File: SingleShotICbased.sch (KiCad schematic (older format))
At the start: 14 parts

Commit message: finished design
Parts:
- added D1, D9: 5.1V, Diode_SMD:D_SOD-123, symbol Device:D_Zener
- added D2, D4, D5, D8: RB751S40T5G, Diode_SMD:D_SOD-523, symbol Device:D_Schottky
- added D3, D6, D7: 2SS100L-W, Diode_SMD:D_SOD-123F, symbol Device:D_Schottky
- added R1: 15K, Resistor_SMD:R_0805_2012Metric_Pad1.15x1.40mm_HandSolder, symbol Device:R
- J1: renamed from J?; value Conn_01x01_Male -> GM_KP_ALIVE; footprint (none) -> Connector_PinHeader_2.54mm:PinHeader_1x01_P2.54mm_Horizontal
- J2: renamed from J?; footprint (none) -> Connector_PinHeader_2.54mm:PinHeader_1x02_P2.54mm_Horizontal
- J3: renamed from J?; value Conn_01x01_Female -> SSR_ANODE; footprint (none) -> Connector_PinHeader_2.54mm:PinHeader_1x01_P2.54mm_Horizontal
- J4: renamed from J?; footprint (none) -> Connector_PinHeader_2.54mm:PinHeader_1x03_P2.54mm_Horizontal
- gave numbers to parts that had none: 10
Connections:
- net Earth: now also C2.2, D1.2 (A), D9.2 (A)
- net LV_BATT+_DIODE: now reaches C1.1, C3.1, U1.1 (IN), U2.1 (IN)
- net LV_BATT+_DIODE: now also D3.1 (K); no longer J2.1 (Pin_1)
- net LIN_TIMER_EN: now reaches U2.2 (EN)
- net LIN_TIMER_EN: now also D6.1 (K), D7.1 (K)
- net LIN_TIMER_VDD: now reaches C4.1, U2.5 (OUT), U2.6 (ADJ/SEN)
- net LIN_TIMER_VDD: now also D5.2 (A); no longer U3.1 (VDD)
- net TIMER_DRVn: now reaches U1.2 (EN), U3.5 (DRVn)
- net LIN_SSR_ANODE: now reaches C2.1, U1.5 (OUT), U1.6 (ADJ/SEN)
- net LIN_SSR_ANODE: now also D4.2 (A)
- net TIMER_DONE: now reaches R4.1, U3.4 (DONE)
- net TIMER_DONE: now also D1.1 (K), R1.1
- net GRND_ESTP: now reaches J4.1 (Pin_1)
- net GRND_ESTP: now also D6.2 (A)
- net PLAT_ESTOP: now reaches J4.2 (Pin_2)
- net PLAT_ESTOP: now also D7.2 (A)
- net TMATICS: now reaches J4.3 (Pin_3)
- net TMATICS: now also D8.2 (A)
- net at J1.1 (Pin_1): now also D2.2 (A), R1.2
- net at J3.1 (Pin_1): now also D2.1 (K), D4.1 (K)
- new net LV_BATT+_RAW: D3.2 (A), J2.1 (Pin_1)
- new net TIMER_VDD: D5.1 (K), D8.1 (K), D9.1 (K), U3.1 (VDD)
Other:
- moved on the sheet: C1, J1, J2, J3, J4, R2, R3, R4, U3

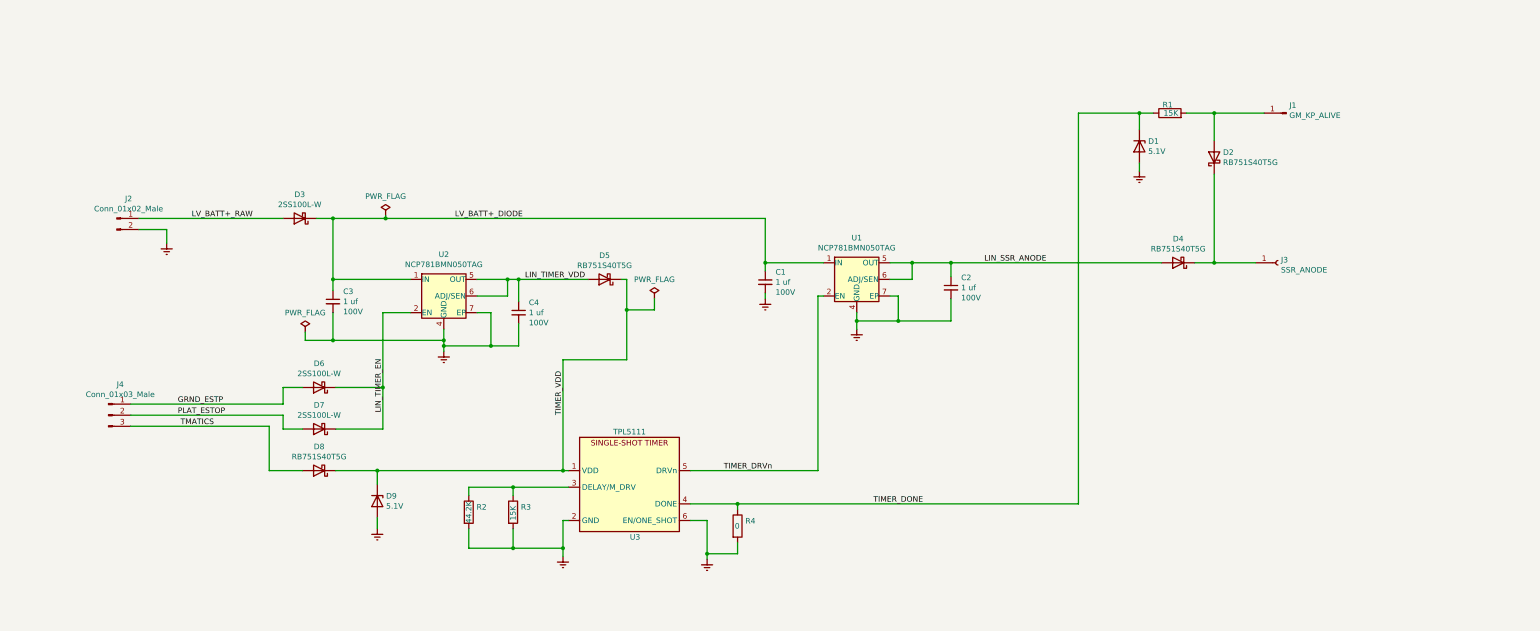
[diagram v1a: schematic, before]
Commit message: bug fixes and design for enclosure
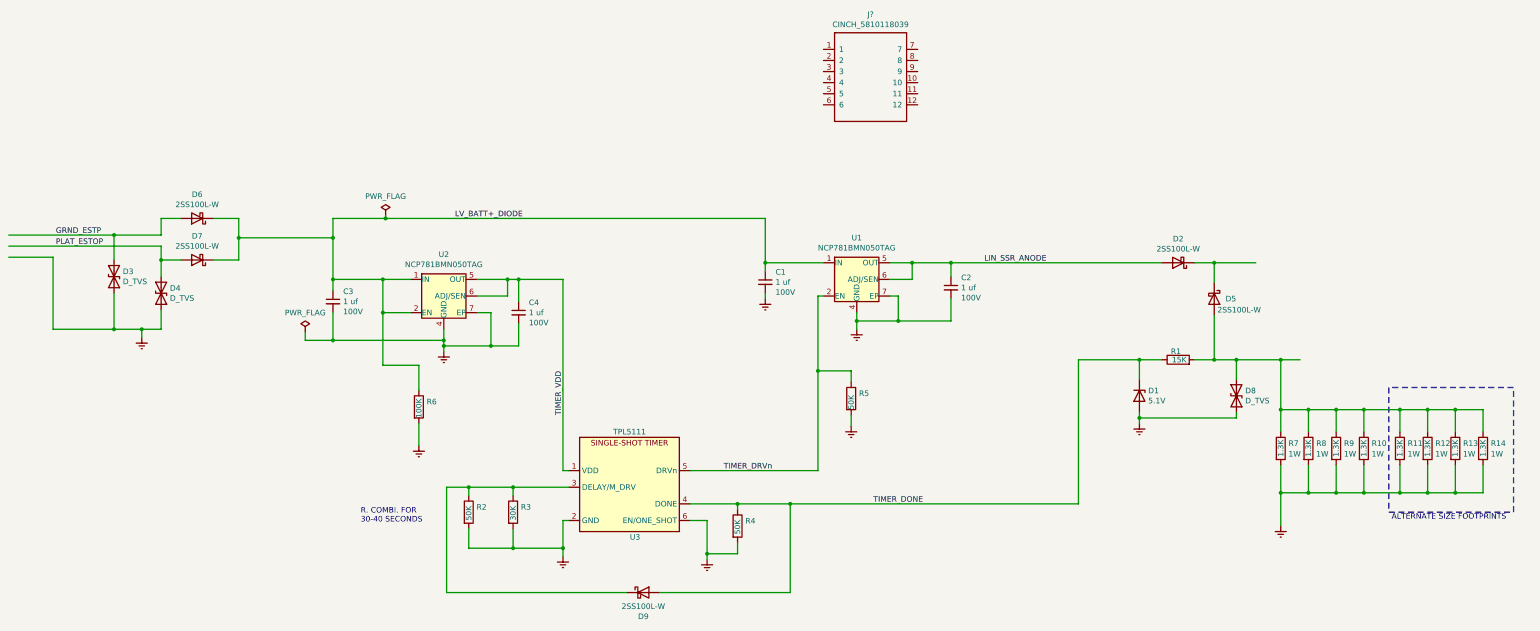
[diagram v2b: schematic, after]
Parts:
- removed D3: 2SS100L-W, Diode_SMD:D_SOD-123F, symbol Device:D_Schottky
- removed D4, D8: RB751S40T5G, Diode_SMD:D_SOD-523, symbol Device:D_Schottky
- removed D9: 5.1V, Diode_SMD:D_SOD-123, symbol Device:D_Zener
- removed J1: GM_KP_ALIVE, Connector_PinHeader_2.54mm:PinHeader_1x01_P2.54mm_Horizontal, symbol Connector:Conn_01x01_Male
- removed J2: Conn_01x02_Male, Connector_PinHeader_2.54mm:PinHeader_1x02_P2.54mm_Horizontal, symbol Connector:Conn_01x02_Male
- removed J3: SSR_ANODE, Connector_PinHeader_2.54mm:PinHeader_1x01_P2.54mm_Horizontal, symbol Connector:Conn_01x01_Female
- removed J4: Conn_01x03_Male, Connector_PinHeader_2.54mm:PinHeader_1x03_P2.54mm_Horizontal, symbol Connector:Conn_01x03_Male
- added D3, D4, D8: D_TVS, Diode_SMD:D_SMB_Handsoldering, symbol Device:D_TVS
- added D9: 2SS100L-W, Diode_SMD:D_SOD-123F, symbol Device:D_Schottky
- added J?: CINCH_5810118039, symbol DWL_Devices:CINCH_5810118039
- added R10, R7, R8, R9: 1.3K, Resistor_SMD:R_1218_3246Metric_Pad1.22x4.75mm_HandSolder, symbol Device:R
- added R11, R12, R13, R14: 1.3K, Resistor_SMD:R_2512_6332Metric_Pad1.52x3.35mm_HandSolder, symbol Device:R
- added R5: 50K, Resistor_SMD:R_0805_2012Metric_Pad1.15x1.40mm_HandSolder, symbol Device:R
- added R6: 100K, Resistor_SMD:R_0805_2012Metric_Pad1.15x1.40mm_HandSolder, symbol Device:R
- D2, D5: value RB751S40T5G -> 2SS100L-W; footprint Diode_SMD:D_SOD-523 -> Diode_SMD:D_SOD-123F; PN RB751S40T5G -> 2SS100L-W
- R2: value 44.2K -> 50K
- R3: value 15K -> 30K
- R4: value 0 -> 50K
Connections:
- net labels removed: LIN_TIMER_EN, LIN_TIMER_VDD, LV_BATT+_RAW, TMATICS
- wire segments 104 -> 154
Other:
- note added: "ALTERNATE SIZE FOOTPRINTS"
- note added: "R. COMBI. FOR\n30-40 SECONDS"
- moved on the sheet: D1, D6, D7, R1
